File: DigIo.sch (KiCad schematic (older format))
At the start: 2 parts

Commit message: Fix Boot0 pin and add prices per component
Signed-off-by: Philip Luyckx <philip.luyckx@gmail.com>
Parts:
- D1: Price (none) -> 0.02
- R2: Price (none) -> 0.01
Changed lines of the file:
@@
 F 2 "Resistors_SMD:R_1206" H 4300 3500 60  0001 C CNN
 F 3 "" H 4300 3500 60  0000 C CNN
+F 4 "0.02" H 4300 3500 60  0001 C CNN "Price"
 	1    4300 3500
 	0    -1   -1   0
@@
 F 2 "Resistors_SMD:R_0603" V 4230 3000 30  0001 C CNN
 F 3 "" H 4300 3000 30  0000 C CNN
+F 4 "0.01" V 4300 3000 60  0001 C CNN "Price"
 	1    4300 3000
 	1    0    0    -1

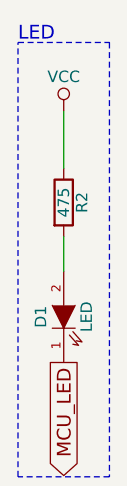
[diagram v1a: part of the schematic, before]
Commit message: Update schematics for V3:
 * Change DHT22 to HTU21D
 * Change schematic for MCP6044
 * Correct unused opamp + power supply
 * Reassign some cpu pins (for HTU21D)
 * Add LDO power supply for 1.8V
 * Update STM32CubeMx project
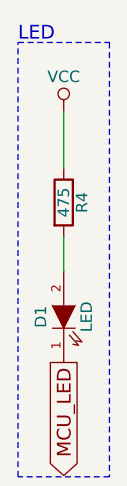
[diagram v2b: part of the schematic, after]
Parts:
- renumbered R2 to R4
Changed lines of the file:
@@
 LIBS:CustomModules
 LIBS:CustomPower
-LIBS:CustomPowerConvertors
 LIBS:CustomTransistors
 LIBS:Custom_ShiftRegisters
@@
 LIBS:Relais
 LIBS:CustomDevices
+LIBS:CustomPowerConvertors
 LIBS:Sensor-cache
 EELAYER 25 0
@@
 $EndComp
 $Comp
-L R R2
+L R R4
 U 1 1 566214E0
 P 4300 3000
-F 0 "R2" V 4380 3000 50  0000 C CNN
+F 0 "R4" V 4380 3000 50  0000 C CNN
 F 1 "475" V 4300 3000 50  0000 C CNN
 F 2 "Resistors_SMD:R_0603" V 4230 3000 30  0001 C CNN
@@
 $EndComp
 $Comp
-L VCC #PWR016
+L VCC #PWR18
 U 1 1 566214F9
 P 4300 2600
-F 0 "#PWR016" H 4300 2450 50  0001 C CNN
+F 0 "#PWR18" H 4300 2450 50  0001 C CNN
 F 1 "VCC" H 4300 2750 50  0000 C CNN
 F 2 "" H 4300 2600 60  0000 C CNN

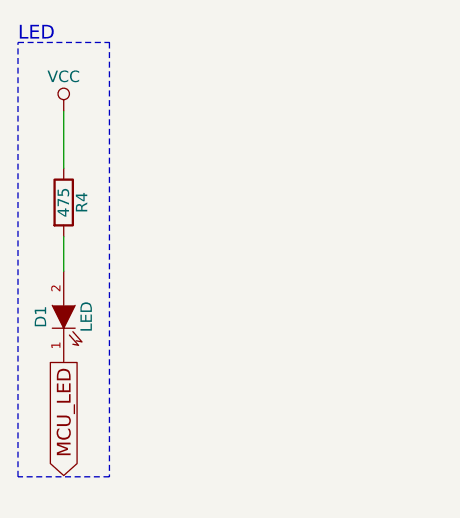
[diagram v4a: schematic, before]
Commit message: Add extra switch for user defined functionality
 * reroute pcb

Signed-off-by: pluyckx <philip.luyckx@gmail.com>
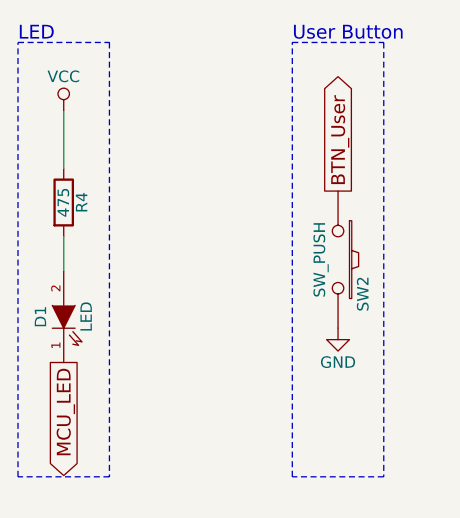
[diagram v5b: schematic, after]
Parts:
- added SW2: SW_PUSH, CustomSmd:MicroSwitch_6x6mm, symbol SW_PUSH
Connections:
- new net BTN_User: SW2.1
- new net GND: SW2.2
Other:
- note added: "User Button"
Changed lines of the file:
@@
 Text Notes 4100 2300 0    60   ~ 0
 LED
+$Comp
+L SW_PUSH SW2
+U 1 1 5791EAD8
+P 5500 3250
+F 0 "SW2" H 5650 3360 50  0000 C CNN
+F 1 "SW_PUSH" H 5500 3170 50  0000 C CNN
+F 2 "CustomSmd:MicroSwitch_6x6mm" H 5500 3250 50  0001 C CNN
+F 3 "" H 5500 3250 50  0000 C CNN
+	1    5500 3250
+	0    1    1    0
+$EndComp
+$Comp
+L GND #PWR019
+U 1 1 5791EB60
+P 5500 3550
+F 0 "#PWR019" H 5500 3300 50  0001 C CNN
+F 1 "GND" H 5500 3400 50  0000 C CNN
+F 2 "" H 5500 3550 50  0000 C CNN
+F 3 "" H 5500 3550 50  0000 C CNN
+	1    5500 3550
+	1    0    0    -1
+$EndComp
+Text GLabel 5500 2950 1    60   Output ~ 0
+BTN_User
+Wire Notes Line
+	5300 4200 5300 2300
+Text Notes 5300 2300 0    60   ~ 0
+User Button
+Wire Notes Line
+	5300 2300 5700 2300
+Wire Notes Line
+	5700 2300 5700 4200
+Wire Notes Line
+	5700 4200 5300 4200
 $EndSCHEMATC

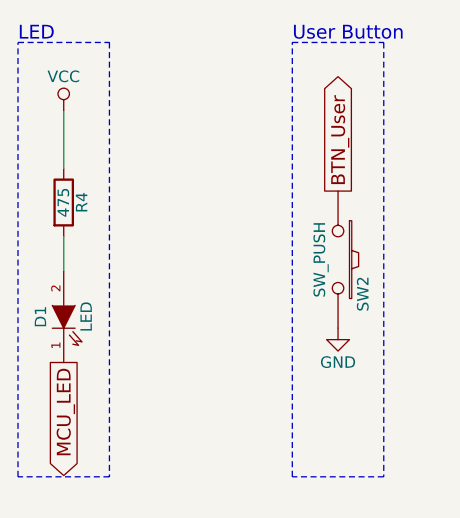
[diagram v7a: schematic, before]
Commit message: Add prices
Signed-off-by: Philip Luyckx <philip.luyckx@gmail.com>
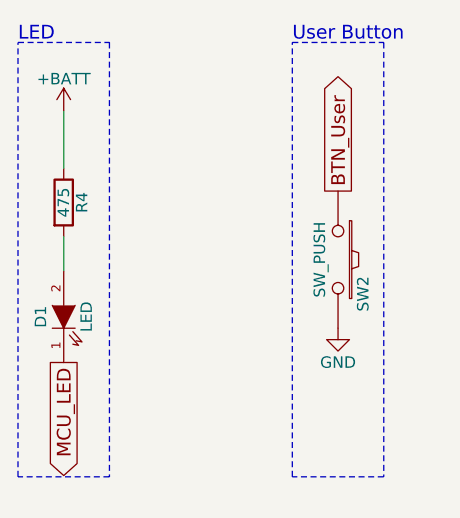
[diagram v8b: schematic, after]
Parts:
- SW2: Price (none) -> 0.05
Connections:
- net VCC renamed +BATT
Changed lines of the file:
@@
-	1    0    0    -1
-$EndComp
-$Comp
-L VCC #PWR020
-U 1 1 566214F9
-P 4300 2600
-F 0 "#PWR020" H 4300 2450 50  0001 C CNN
-F 1 "VCC" H 4300 2750 50  0000 C CNN
-F 2 "" H 4300 2600 60  0000 C CNN
-F 3 "" H 4300 2600 60  0000 C CNN
-	1    4300 2600
 	1    0    0    -1
 $EndComp
@@
 F 2 "CustomSmd:MicroSwitch_6x6mm" H 5500 3250 50  0001 C CNN
 F 3 "" H 5500 3250 50  0000 C CNN
+F 4 "0.05" H 5500 3250 60  0001 C CNN "Price"
 	1    5500 3250
 	0    1    1    0
 $EndComp
 $Comp
-L GND #PWR021
+L GND #PWR020
 U 1 1 5791EB60
 P 5500 3550
-F 0 "#PWR021" H 5500 3300 50  0001 C CNN
+F 0 "#PWR020" H 5500 3300 50  0001 C CNN
 F 1 "GND" H 5500 3400 50  0000 C CNN
 F 2 "" H 5500 3550 50  0000 C CNN
@@
 Wire Notes Line
 	5700 4200 5300 4200
+$Comp
+L +BATT #PWR021
+U 1 1 58A78F16
+P 4300 2600
+F 0 "#PWR021" H 4300 2450 50  0001 C CNN
+F 1 "+BATT" H 4300 2740 50  0000 C CNN
+F 2 "" H 4300 2600 50  0000 C CNN
+F 3 "" H 4300 2600 50  0000 C CNN
+	1    4300 2600
+	1    0    0    -1
+$EndComp
 $EndSCHEMATC
